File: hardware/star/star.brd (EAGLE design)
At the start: 139.4 x 187.9 mm, 160 parts, among them IC1 MAX481CSA, IC2 74HCT08D, IC22 LD117AS12TR, IC3 74HCT08D, IC4 7404D, IC8 MAX481CSA, K1 T90-12VDC-TL-A, K2 T90-12VDC-TL-A, K3 T90-12VDC-TL-A, K5 AQG22110, K6 AQG22110, Q1 35A/25V/8.5mΩ, Q2 35A/25V/8.5mΩ, Q3 35A/25V/8.5mΩ, Q4 35A/25V/8.5mΩ, U1 TCLT1600, U2 ADXL343BCCZ-RL7, U3 TMP102AIDRLR, U4 SN74LVC1G17DCK, U5 SN74LVC1G17DCK, U6 SN74LVC1G17DCK, U7 SN74LVC1G17DCK, X1 MKDSN1,5/2-5,08

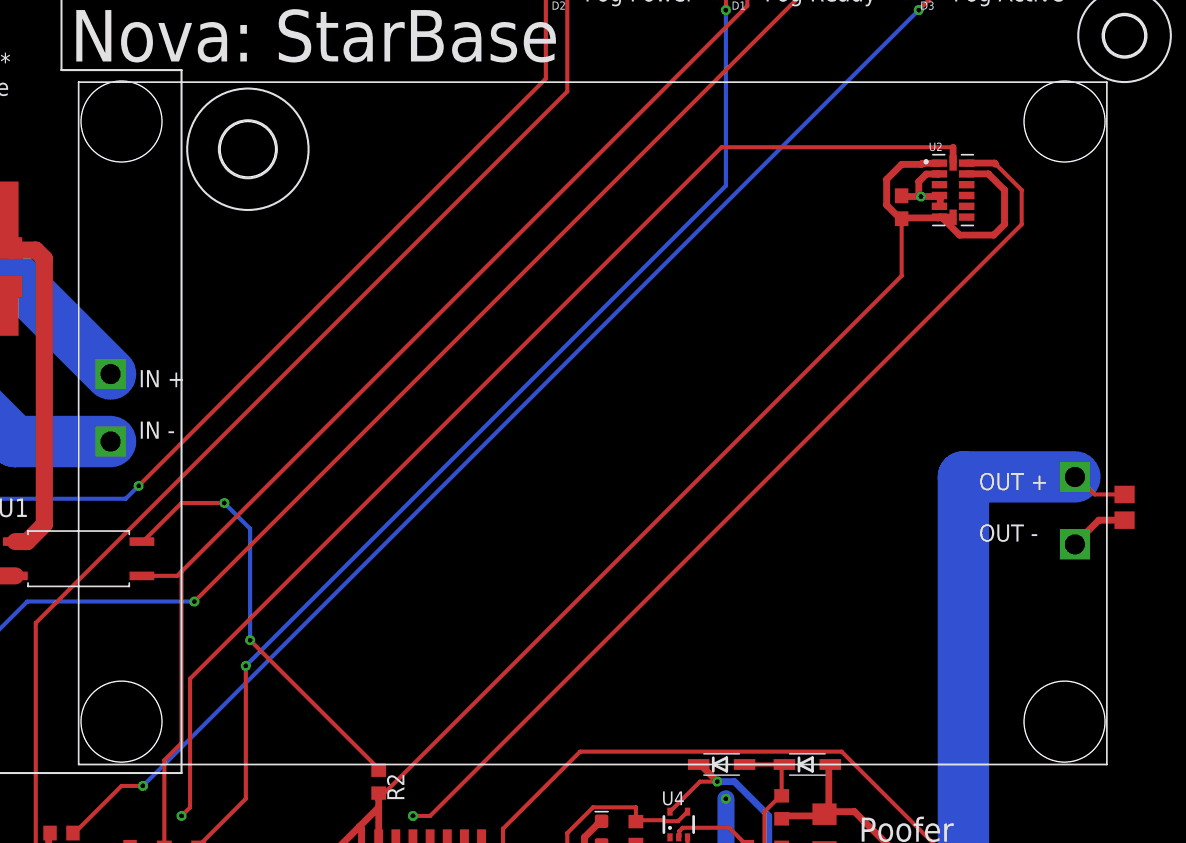
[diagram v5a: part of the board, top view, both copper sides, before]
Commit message: change hole size
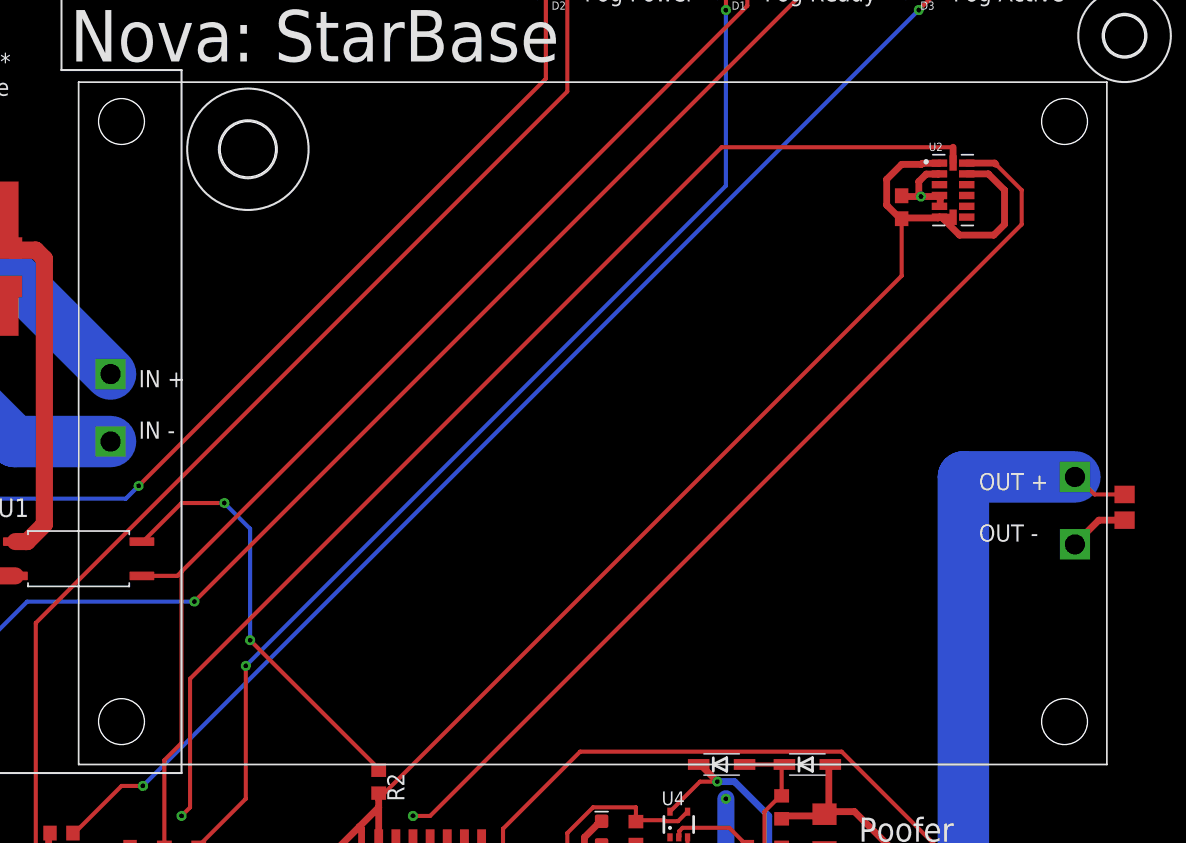
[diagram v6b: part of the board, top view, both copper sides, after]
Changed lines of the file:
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@@
 <wire x1="105.7275" y1="100.0125" x2="106.68" y2="100.0125" width="0.3048" layer="1"/>
 <wire x1="103.82" y1="101.92" x2="105.7275" y2="100.0125" width="0.3048" layer="1"/>
+<wire x1="126.365" y1="113.665" x2="132.715" y2="112.49" width="0" layer="19" extent="1-1"/>
+<wire x1="106.68" y1="121.07" x2="109.22" y2="124.88" width="0" layer="19" extent="1-1"/>
+<wire x1="113.46" y1="107.95" x2="112.395" y2="114.43" width="0" layer="19" extent="1-1"/>
+<wire x1="106.68" y1="89.955" x2="109.22" y2="93.765" width="0" layer="19" extent="1-1"/>
+<wire x1="86.36" y1="75.985" x2="83.285" y2="78.875" width="0" layer="19" extent="1-1"/>
+<wire x1="121.66" y1="90.17" x2="121.66" y2="95.885" width="0" layer="19" extent="1-1"/>
+<wire x1="121.66" y1="72.39" x2="121.66" y2="76.835" width="0" layer="19" extent="1-1"/>
+<wire x1="99.22" y1="73.66" x2="90.01" y2="76.2" width="0" layer="19" extent="1-1"/>
+<wire x1="106.2228" y1="71.12" x2="99.22" y2="71.12" width="0" layer="19" extent="1-1"/>
+<wire x1="131.445" y1="85.09" x2="121.66" y2="85.725" width="0" layer="19" extent="1-1"/>
+<wire x1="135.5725" y1="87.3125" x2="131.445" y2="85.09" width="0" layer="19" extent="1-1"/>
+<wire x1="137.16" y1="98.005" x2="137.16" y2="87.31" width="0" layer="19" extent="1-1"/>
+<wire x1="95.68" y1="53.35" x2="86.995" y2="62.3316" width="0" layer="19" extent="1-1"/>
+<wire x1="102.87" y1="53.76" x2="95.68" y2="53.35" width="0" layer="19" extent="1-1"/>
+<wire x1="132.715" y1="65.39" x2="121.66" y2="72.39" width="0" layer="19" extent="1-1"/>
+<wire x1="120.45" y1="53.35" x2="132.715" y2="65.39" width="0" layer="19" extent="1-1"/>
+<wire x1="132.715" y1="35.465" x2="120.45" y2="53.35" width="0" layer="19" extent="1-1"/>
+<wire x1="133.35" y1="13.335" x2="125.945" y2="20.32" width="0" layer="19" extent="1-1"/>
+<wire x1="125.095" y1="2.54" x2="133.35" y2="13.335" width="0" layer="19" extent="1-1"/>
+<wire x1="109.22" y1="8.57" x2="125.095" y2="2.54" width="0" layer="19" extent="1-1"/>
+<wire x1="130.945" y1="145.205" x2="112.825" y2="128.905" width="0" layer="19" extent="1-1"/>
+<wire x1="120.91" y1="170.25" x2="130.945" y2="145.205" width="0" layer="19" extent="1-1"/>
+<wire x1="51.435" y1="5.715" x2="90.17" y2="6.22" width="0" layer="19" extent="1-1"/>
+<wire x1="36.83" y1="5.715" x2="51.435" y2="5.715" width="0" layer="19" extent="1-1"/>
+<wire x1="50.83" y1="23.51" x2="51.435" y2="5.715" width="0" layer="19" extent="1-1"/>
+<wire x1="50.83" y1="35.575" x2="50.83" y2="23.51" width="0" layer="19" extent="1-1"/>
+<wire x1="25.43" y1="23.51" x2="36.83" y2="5.715" width="0" layer="19" extent="1-1"/>
+<wire x1="25.43" y1="35.575" x2="25.43" y2="23.51" width="0" layer="19" extent="1-1"/>
+<wire x1="15.66" y1="9.525" x2="25.43" y2="23.51" width="0" layer="19" extent="1-1"/>
+<wire x1="7.595" y1="37.4439" x2="7.595" y2="20.9339" width="0" layer="19" extent="1-1"/>
+<wire x1="7.595" y1="47.6039" x2="7.595" y2="37.4439" width="0" layer="19" extent="1-1"/>
+<wire x1="6.985" y1="66.04" x2="7.595" y2="47.6039" width="0" layer="19" extent="1-1"/>
+<wire x1="29.27" y1="58.46" x2="8.89" y2="66.04" width="0" layer="19" extent="1-1"/>
 </signal>
 <signal name="N$1">

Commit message: Starbase 1.3.0 Final
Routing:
- net +24V: track 359.9 -> 372.2 mm, vias 2 -> 1
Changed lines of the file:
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@@
 </polygon>
 <text x="138.43" y="16.51" size="1.016" layer="21" rot="R180">3v3 GND SCL SDA</text>
-<rectangle x1="34.29" y1="160.655" x2="41.275" y2="164.465" layer="1"/>
-<rectangle x1="40.64" y1="167.005" x2="46.99" y2="172.085" layer="1"/>
-<rectangle x1="45.72" y1="160.655" x2="52.705" y2="164.465" layer="1"/>
+<rectangle x1="34.29" y1="160.02" x2="41.275" y2="163.83" layer="1"/>
+<rectangle x1="40.64" y1="167.64" x2="46.99" y2="172.72" layer="1"/>
+<rectangle x1="45.72" y1="160.02" x2="52.705" y2="163.83" layer="1"/>
 <text x="3.175" y="74.295" size="2.54" layer="21" rot="R90">+    -</text>
-<rectangle x1="34.29" y1="167.005" x2="37.465" y2="172.085" layer="1"/>
-<rectangle x1="49.53" y1="167.005" x2="52.705" y2="172.085" layer="1"/>
+<rectangle x1="34.29" y1="167.64" x2="37.465" y2="172.72" layer="1"/>
+<rectangle x1="49.53" y1="167.64" x2="52.705" y2="172.72" layer="1"/>
 <text x="94.615" y="185.42" size="1.27" layer="21">Fog Power</text>
 <text x="107.95" y="185.42" size="1.27" layer="21">Fog Ready</text>
@@
 <contactref element="C4" pad="2"/>
 <contactref element="U3" pad="4"/>
-<via x="76.2" y="90.17" extent="1-16" drill="1"/>
+<via x="76.2" y="90.17" extent="1-16" drill="1.27"/>
 <wire x1="120.80875" y1="170.97375" x2="119.53875" y2="170.97375" width="0.508" layer="1"/>
 <wire x1="119.53875" y1="170.97375" x2="118.11" y2="170.97375" width="0.508" layer="1"/>
@@
 <wire x1="105.7275" y1="100.0125" x2="106.68" y2="100.0125" width="0.3048" layer="1"/>
 <wire x1="103.82" y1="101.92" x2="105.7275" y2="100.0125" width="0.3048" layer="1"/>
-<wire x1="126.365" y1="113.665" x2="132.715" y2="112.49" width="0" layer="19" extent="1-1"/>
-<wire x1="106.68" y1="121.07" x2="109.22" y2="124.88" width="0" layer="19" extent="1-1"/>
-<wire x1="113.46" y1="107.95" x2="112.395" y2="114.43" width="0" layer="19" extent="1-1"/>
-<wire x1="106.68" y1="89.955" x2="109.22" y2="93.765" width="0" layer="19" extent="1-1"/>
-<wire x1="86.36" y1="75.985" x2="83.285" y2="78.875" width="0" layer="19" extent="1-1"/>
-<wire x1="121.66" y1="90.17" x2="121.66" y2="95.885" width="0" layer="19" extent="1-1"/>
-<wire x1="121.66" y1="72.39" x2="121.66" y2="76.835" width="0" layer="19" extent="1-1"/>
-<wire x1="99.22" y1="73.66" x2="90.01" y2="76.2" width="0" layer="19" extent="1-1"/>
-<wire x1="106.2228" y1="71.12" x2="99.22" y2="71.12" width="0" layer="19" extent="1-1"/>
-<wire x1="131.445" y1="85.09" x2="121.66" y2="85.725" width="0" layer="19" extent="1-1"/>
-<wire x1="135.5725" y1="87.3125" x2="131.445" y2="85.09" width="0" layer="19" extent="1-1"/>
-<wire x1="137.16" y1="98.005" x2="137.16" y2="87.31" width="0" layer="19" extent="1-1"/>
-<wire x1="95.68" y1="53.35" x2="86.995" y2="62.3316" width="0" layer="19" extent="1-1"/>
-<wire x1="102.87" y1="53.76" x2="95.68" y2="53.35" width="0" layer="19" extent="1-1"/>
-<wire x1="132.715" y1="65.39" x2="121.66" y2="72.39" width="0" layer="19" extent="1-1"/>
-<wire x1="120.45" y1="53.35" x2="132.715" y2="65.39" width="0" layer="19" extent="1-1"/>
-<wire x1="132.715" y1="35.465" x2="120.45" y2="53.35" width="0" layer="19" extent="1-1"/>
-<wire x1="133.35" y1="13.335" x2="125.945" y2="20.32" width="0" layer="19" extent="1-1"/>
-<wire x1="125.095" y1="2.54" x2="133.35" y2="13.335" width="0" layer="19" extent="1-1"/>
-<wire x1="109.22" y1="8.57" x2="125.095" y2="2.54" width="0" layer="19" extent="1-1"/>
-<wire x1="130.945" y1="145.205" x2="112.825" y2="128.905" width="0" layer="19" extent="1-1"/>
-<wire x1="120.91" y1="170.25" x2="130.945" y2="145.205" width="0" layer="19" extent="1-1"/>
-<wire x1="51.435" y1="5.715" x2="90.17" y2="6.22" width="0" layer="19" extent="1-1"/>
-<wire x1="36.83" y1="5.715" x2="51.435" y2="5.715" width="0" layer="19" extent="1-1"/>
-<wire x1="50.83" y1="23.51" x2="51.435" y2="5.715" width="0" layer="19" extent="1-1"/>
-<wire x1="50.83" y1="35.575" x2="50.83" y2="23.51" width="0" layer="19" extent="1-1"/>
-<wire x1="25.43" y1="23.51" x2="36.83" y2="5.715" width="0" layer="19" extent="1-1"/>
-<wire x1="25.43" y1="35.575" x2="25.43" y2="23.51" width="0" layer="19" extent="1-1"/>
-<wire x1="15.66" y1="9.525" x2="25.43" y2="23.51" width="0" layer="19" extent="1-1"/>
-<wire x1="7.595" y1="37.4439" x2="7.595" y2="20.9339" width="0" layer="19" extent="1-1"/>
-<wire x1="7.595" y1="47.6039" x2="7.595" y2="37.4439" width="0" layer="19" extent="1-1"/>
-<wire x1="6.985" y1="66.04" x2="7.595" y2="47.6039" width="0" layer="19" extent="1-1"/>
-<wire x1="29.27" y1="58.46" x2="8.89" y2="66.04" width="0" layer="19" extent="1-1"/>
 </signal>
 <signal name="N$1">
@@
 <contactref element="FIRE_OUT" pad="3"/>
 <contactref element="D17" pad="A"/>
-<wire x1="7.595" y1="86.3389" x2="13.3561" y2="86.3389" width="2.54" layer="16"/>
-<wire x1="13.3561" y1="86.3389" x2="17.145" y2="82.55" width="2.54" layer="16"/>
-<wire x1="17.145" y1="82.55" x2="17.145" y2="71.12" width="2.54" layer="16"/>
 <contactref element="X1" pad="2"/>
 <wire x1="132.3975" y1="148.9075" x2="134.62" y2="148.9075" width="0.3048" layer="1"/>
@@
 <wire x1="55.972490625" y1="35.71875" x2="54.61" y2="35.71875" width="0.3048" layer="16"/>
 <wire x1="29.27" y1="53.4" x2="37.5417125" y2="53.4" width="3.81" layer="16"/>
-<via x="17.145" y="71.12" extent="1-16" drill="2.54"/>
-<wire x1="17.145" y1="71.12" x2="17.145" y2="62.865" width="2.54" layer="1"/>
-<wire x1="17.145" y1="62.865" x2="26.67" y2="53.34" width="2.54" layer="1"/>
-<wire x1="26.67" y1="53.34" x2="29.21" y2="53.34" width="2.54" layer="1"/>
+<wire x1="20.32" y1="53.34" x2="15.24" y2="58.42" width="2.54" layer="1"/>
+<wire x1="29.21" y1="53.34" x2="20.32" y2="53.34" width="2.54" layer="1"/>
 <wire x1="29.21" y1="53.34" x2="29.27" y2="53.4" width="2.54" layer="1"/>
 <wire x1="55.88" y1="35.56" x2="55.91" y2="35.575" width="0.3048" layer="16"/>
 <wire x1="55.88" y1="35.56" x2="54.61" y2="36.35375" width="0.3048" layer="16"/>
+<wire x1="15.24" y1="58.42" x2="5.08" y2="58.42" width="2.54" layer="1"/>
+<wire x1="5.08" y1="58.42" x2="2.286" y2="61.214" width="2.54" layer="1"/>
+<wire x1="2.286" y1="61.214" x2="2.286" y2="83.82" width="2.54" layer="1"/>
+<wire x1="2.286" y1="83.82" x2="4.8049" y2="86.3389" width="2.54" layer="1"/>
+<wire x1="4.8049" y1="86.3389" x2="7.595" y2="86.3389" width="2.54" layer="1"/>
 <wire x1="58.42" y1="84.1375" x2="58.89625" y2="83.66125" width="0" layer="19" extent="1-1"/>
 </signal>

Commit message: Initial code for starbase
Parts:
- R15: value R_1K_0603 -> R_2K_0603
- moved NID35-12 1.27 mm to (14.0, 15.2)
- moved NID35-5 1.27 mm to (14.0, 27.3)
- renumbered R63 to R15
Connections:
- net +12V: now also D15.C, D16.A, K3.1
- net +5V: no longer D15.C, D16.A, K3.1
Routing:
- net +12V: track 319.8 -> 367.3 mm
- net +5V: track 525.7 -> 494.2 mm, vias 3 -> 2
- net +24V: track 372.2 -> 376.4 mm
- net EN_STATUS: track 142.2 -> 142.9 mm
